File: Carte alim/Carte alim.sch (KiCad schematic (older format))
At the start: 34 parts, among them P1 CONN_2, P10 CONN_2, P11 CONN_2, P12 CONN_2, P13 CONN_2, P14 CONN_2, P15 CONN_8, P16 CONN_8, P2 CONN_2, P3 CONN_2, P4 CONN_2, P5 CONN_2, P6 CONN_2, P7 CONN_2, P8 CONN_2, P9 CONN_2, U1 78033, U2 7805

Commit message: Rajout de pins d'alimentation et modification du typon en conséquence
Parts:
- added P17, P18, P19, P20, P21, P22, P23, P24, P25, P26, P27, P28, P29: CONN_2, symbol CONN_2
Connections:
- net +3.3V: now also P22.1 (P1), P23.1 (P1), P24.1 (P1), P25.1 (P1), P26.1 (P1)
- net +5V: now also P17.1 (P1), P18.1 (P1), P19.1 (P1), P20.1 (P1), P21.1 (P1)
- net +BATT: now also P27.1 (P1), P28.1 (P1), P29.1 (P1)
- net GND: now also P17.2 (PM), P18.2 (PM), P19.2 (PM), P20.2 (PM), P21.2 (PM), P22.2 (PM), P23.2 (PM), P24.2 (PM), P25.2 (PM), P26.2 (PM), P27.2 (PM), P28.2 (PM), P29.2 (PM)
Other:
- note added: "Connecteurs pour branchement vers autres cartes\n(on double pour prévoir large pour les années suivantes)"

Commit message: Correction empreinte régulateur 3.3V
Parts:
- removed U1: 78033, symbol 78033
- added U1: LM317T, symbol LM317T
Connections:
- net +3.3V: now also U1.2 (Out)
- net +BATT: now also U1.3 (IN)
- net GND: now also U1.1 (Adj)
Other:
- note added: "OK nums pins"

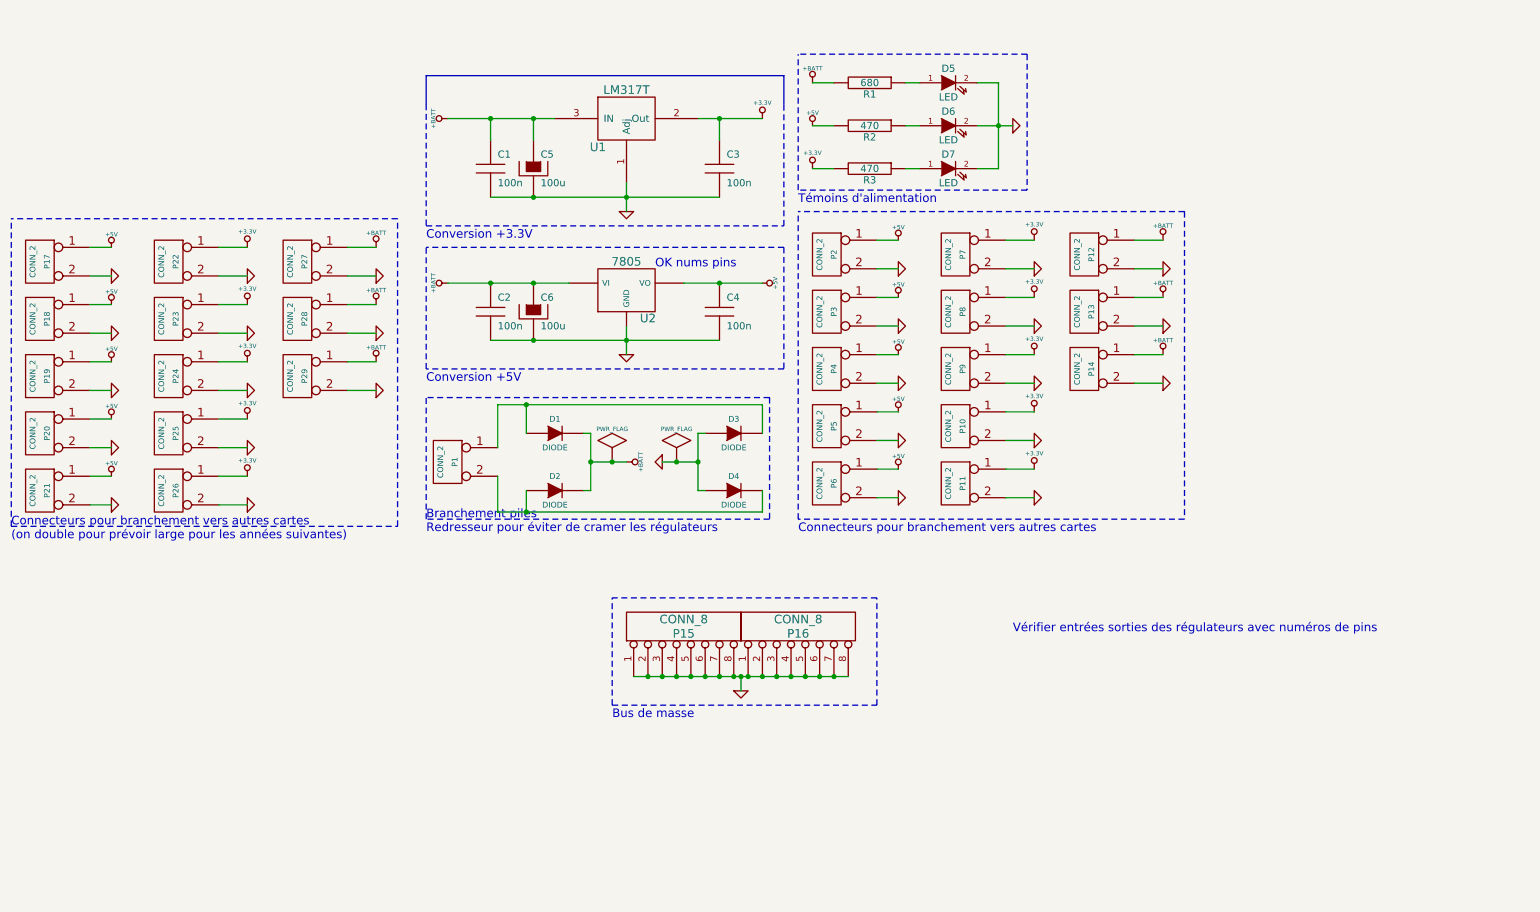
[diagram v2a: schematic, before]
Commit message: Composants valués + rajout condos polarisés en sortie des régulateurs
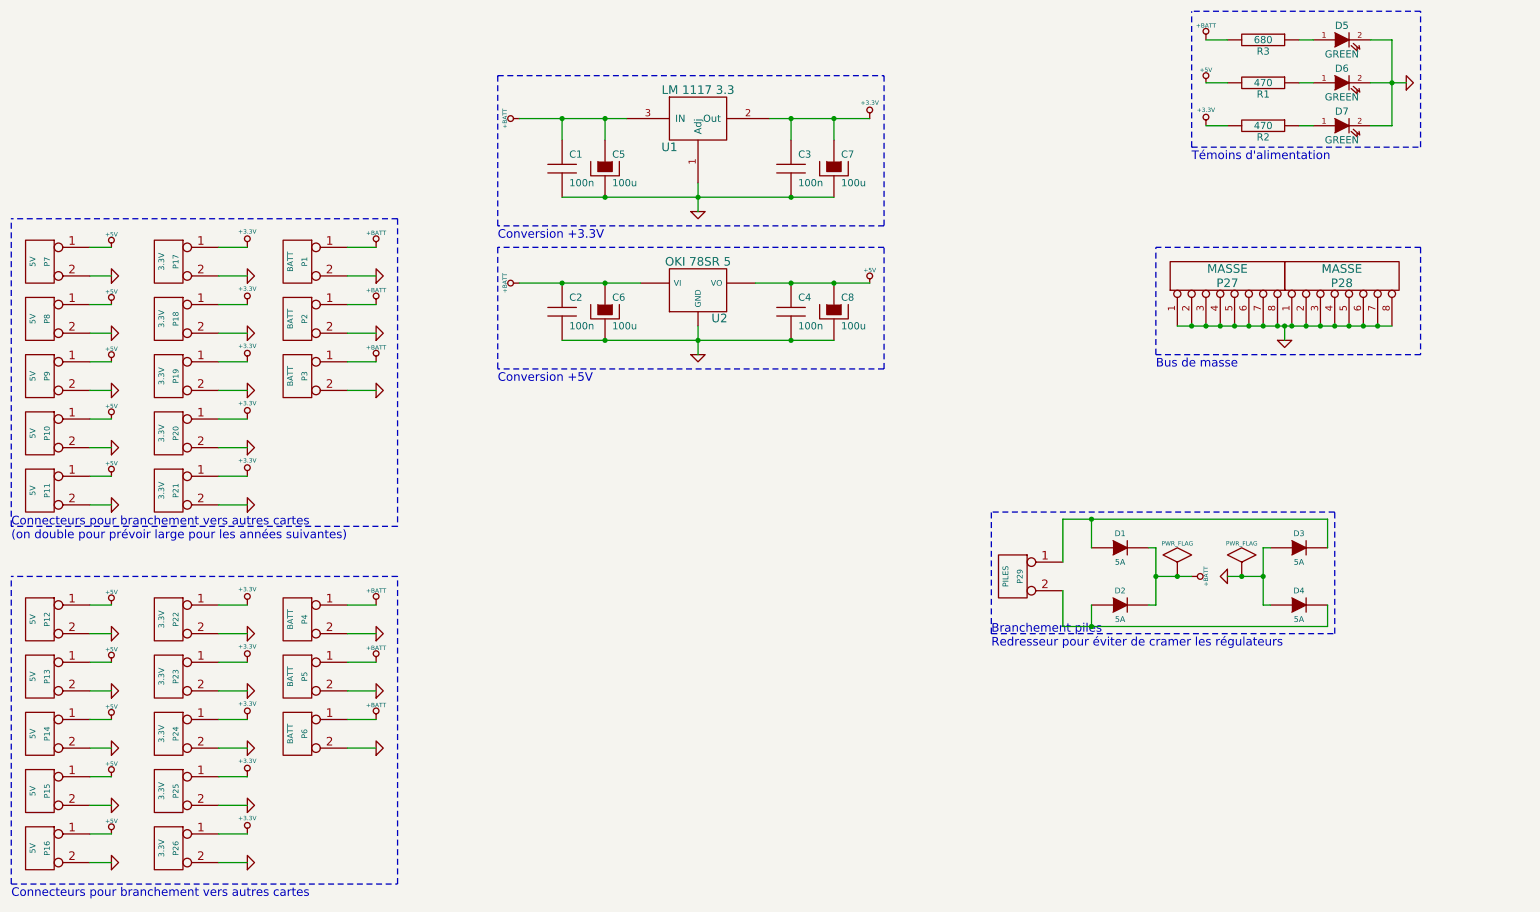
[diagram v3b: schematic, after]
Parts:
- removed P27, P28, P3, P7: CONN_2, symbol CONN_2
- added C7, C8: 100u, symbol CAPAPOL
- added P1: BATT, symbol CONN_2
- added P15, P16: 5V, symbol CONN_2
- added P22: 3.3V, symbol CONN_2
- D1, D2, D3, D4: value DIODE -> 5A
- D5, D6, D7: value LED -> GREEN
- P10, P11, P12, P13, P14, P8, P9: value CONN_2 -> 5V
- P17: renamed from P22; value CONN_2 -> 3.3V
- P18, P19, P20, P21, P23, P24, P25, P26: value CONN_2 -> 3.3V
- P2, P4, P5, P6: value CONN_2 -> BATT
- P27: renamed from P15; value CONN_8 -> MASSE
- P28: renamed from P16; value CONN_8 -> MASSE
- P29: renamed from P1; value CONN_2 -> PILES
- P3: renamed from P29; value CONN_2 -> BATT
- P7: renamed from P17; value CONN_2 -> 5V
- U1: value LM317T -> LM 1117 3.3
- U2: value 7805 -> OKI 78SR 5
- renumbered R2 to R1, R3 to R2, R1 to R3
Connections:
- net +3.3V: now also P18.1 (P1), P19.1 (P1), P20.1 (P1), P21.1 (P1), C7.1, P22.1 (P1); no longer P10.1 (P1), P11.1 (P1), P8.1 (P1), P9.1 (P1)
- net +5V: now also P10.1 (P1), P11.1 (P1), P12.1 (P1), P13.1 (P1), P14.1 (P1), P8.1 (P1), P9.1 (P1), C8.1, P15.1 (P1), P16.1 (P1); no longer P18.1 (P1), P19.1 (P1), P2.1 (P1), P20.1 (P1), P21.1 (P1), P4.1 (P1), P5.1 (P1), P6.1 (P1)
- net +BATT: now also P2.1 (P1), P4.1 (P1), P5.1 (P1), P6.1 (P1), P1.1 (P1); no longer P12.1 (P1), P13.1 (P1), P14.1 (P1)
- net GND: now also C7.2, C8.2, P1.2 (PM), P15.2 (PM), P16.2 (PM), P22.2 (PM)
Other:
- note removed: "OK nums pins"
- note removed: "Vérifier entrées sorties des régulateurs avec numéros de pins"
- moved on the sheet: C1, C2, C3, C4, C5, C6, D1, D5, P27, P28, P29, R1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

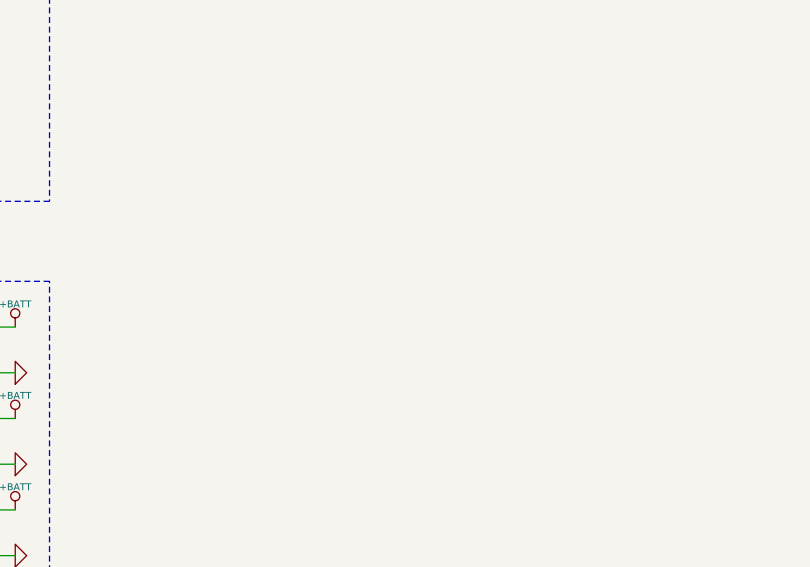
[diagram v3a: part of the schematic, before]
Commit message: Ajout de trous de fixation
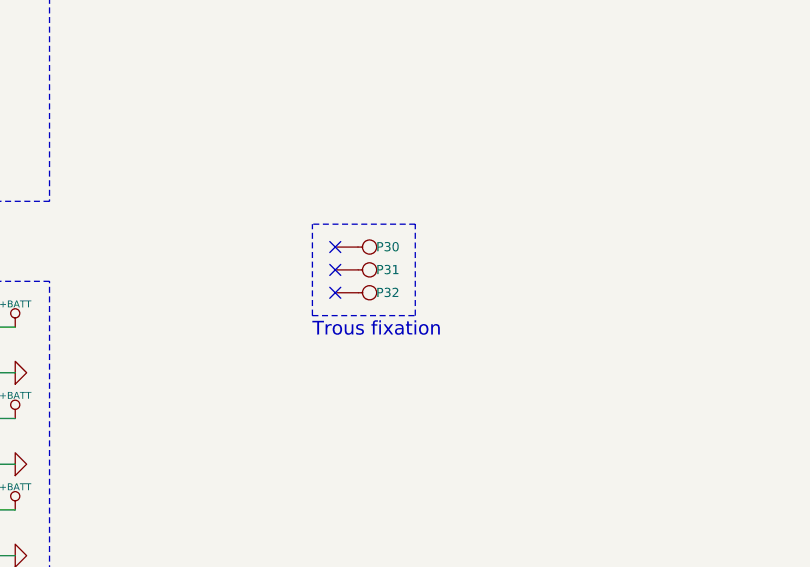
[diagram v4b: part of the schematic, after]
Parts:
- added P30, P31, P32: CONN_1, symbol CONN_1
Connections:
- no-connect marks 0 -> 3
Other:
- note added: "Trous fixation"
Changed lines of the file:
@@
-EESchema Schematic File Version 2  date 07/02/2018 16:51:36
+EESchema Schematic File Version 2  date 07/02/2018 17:43:41
 LIBS:power
 LIBS:device
@@
 $EndDescr
 Wire Notes Line
+	4650 5000 4650 4600
+Wire Notes Line
+	4650 5000 5100 5000
+Wire Notes Line
+	5100 5000 5100 4600
+Wire Notes Line
 	6900 3400 4200 3400
 Wire Notes Line
@@
 Wire Notes Line
 	6900 2400 4200 2400
+Wire Notes Line
+	5100 4600 4650 4600
+Text Notes 4650 5100 0    60   ~ 0
+Trous fixation
+NoConn ~ 4750 4900
+NoConn ~ 4750 4800
+NoConn ~ 4750 4700
+$Comp
+L CONN_1 P32
+U 1 1 5A7B2BAF
+P 4900 4900
+F 0 "P32" H 4980 4900 40  0000 C CNN
+F 1 "CONN_1" H 4850 4940 30  0001 C CNN
+	1    4900 4900
+	1    0    0    -1
+$EndComp
+$Comp
+L CONN_1 P31
+U 1 1 5A7B2BAE
+P 4900 4800
+F 0 "P31" H 4980 4800 40  0000 C CNN
+F 1 "CONN_1" H 4850 4840 30  0001 C CNN
+	1    4900 4800
+	1    0    0    -1
+$EndComp
+$Comp
+L CONN_1 P30
+U 1 1 5A7B2BAA
+P 4900 4700
+F 0 "P30" H 4980 4700 40  0000 C CNN
+F 1 "CONN_1" H 4850 4740 30  0001 C CNN
+	1    4900 4700
+	1    0    0    -1
+$EndComp
 $Comp
 L CAPAPOL C8
